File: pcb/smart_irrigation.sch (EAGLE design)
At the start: 33 parts, among them IC1 TMP36, IC2 7805DT, IC3 7833DT, IC4 DS1307, Q1 IRF730, Q2 32.768, T1 2N3904, U1 BL600

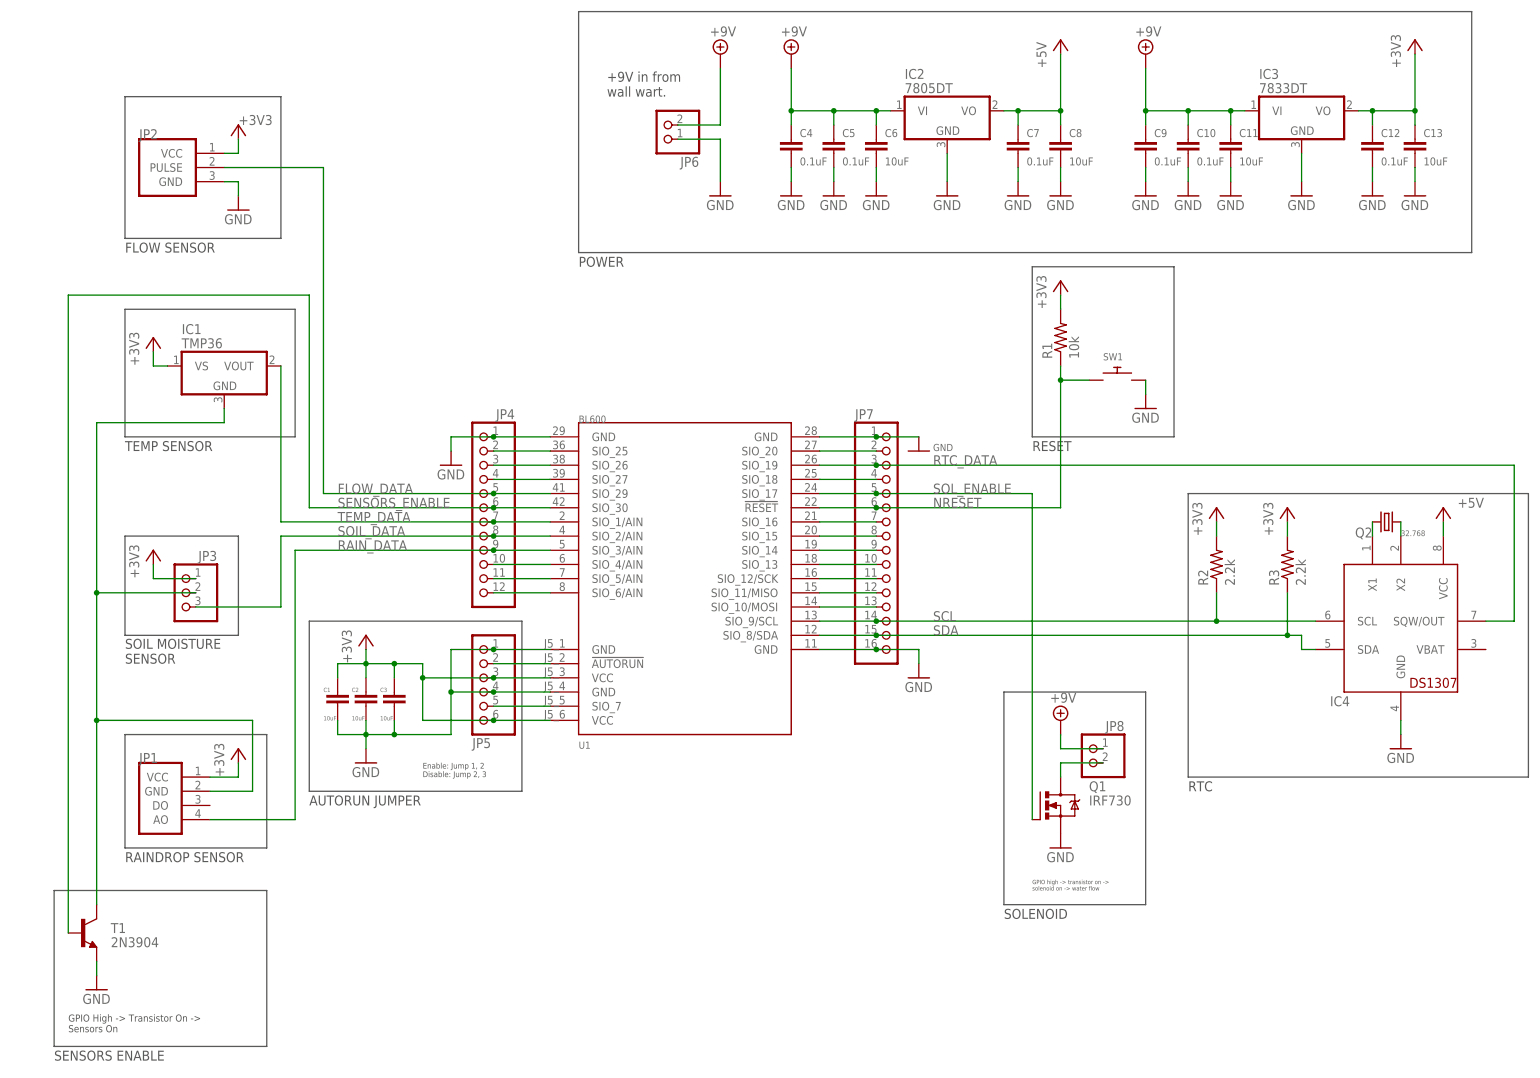
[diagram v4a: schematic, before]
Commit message: PCB: Change sensor pin assignments
All digital sensor outputs are now in one cluster and all analog sensor
outputs are in another cluster.
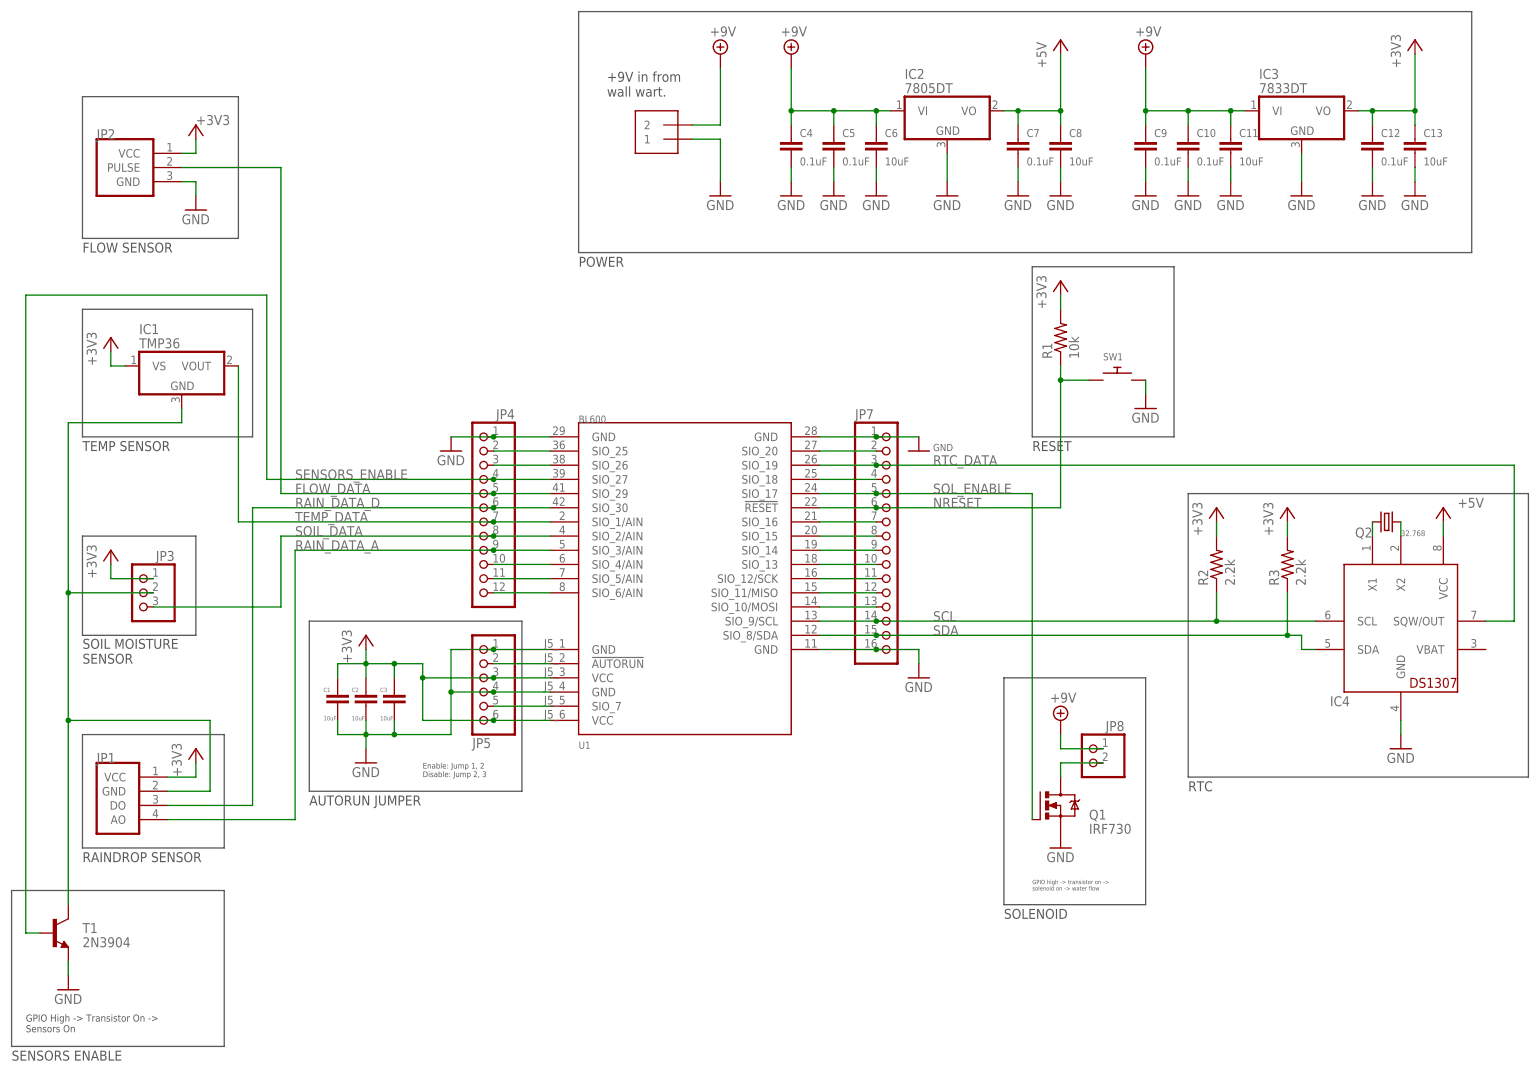
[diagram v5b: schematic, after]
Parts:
- JP6: value (none) -> 1X2-3.5MM; device pinhead:PINHD-1X2 -> adafruit:1X2-3.5MM
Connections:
- net RAIN_DATA renamed RAIN_DATA_A
- removed net SIO_27: JP4.4, U1.SIO_27
- new net RAIN_DATA_D: JP1.DO, JP4.6, U1.SIO_30
- net SENSORS_ENABLE: now also JP4.4, U1.SIO_27; no longer JP4.6, U1.SIO_30
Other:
- moved on the sheet: IC1, JP1, JP2, JP3, T1

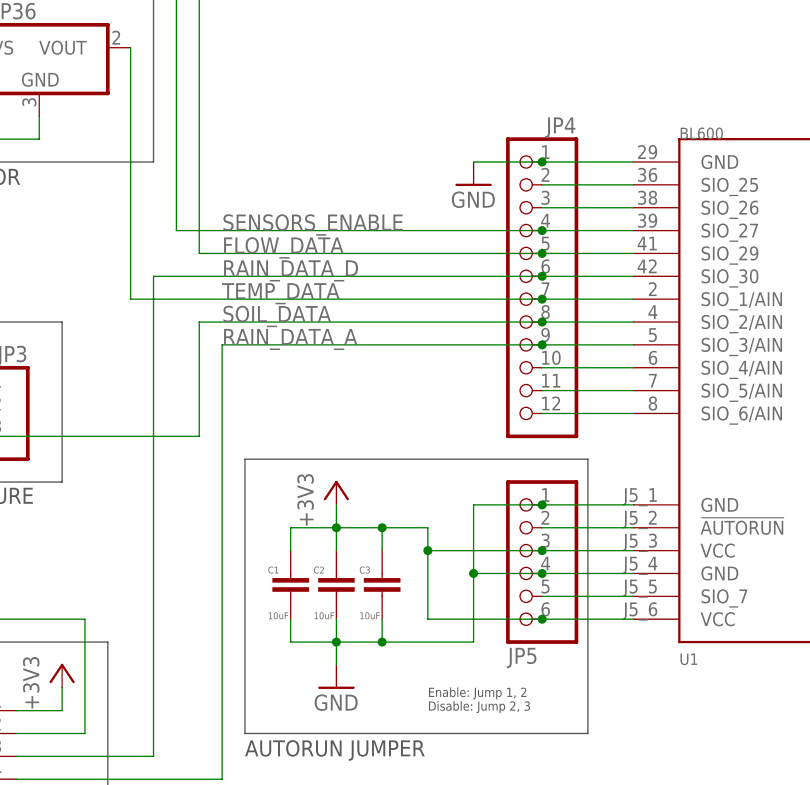
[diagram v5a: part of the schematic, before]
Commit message: PCB: Change SENSORS_ENABLE signal pin
The BL600 breakout board includes SIO_26 and SIO_27, but they're
reserved and unusable for some reason. SENSORS_ENABLE was thus changed
from SIO_27 to SIO_25.
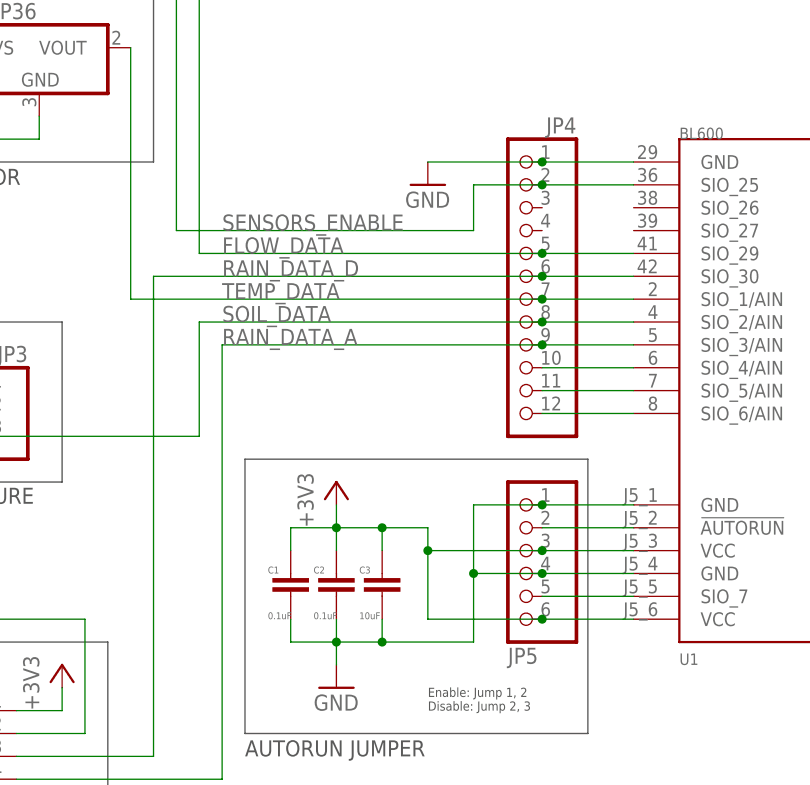
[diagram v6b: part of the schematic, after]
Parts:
- C1, C2: value 10uF -> 0.1uF
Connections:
- removed net SIO_25: JP4.2, U1.SIO_25
- removed net SIO_26: JP4.3, U1.SIO_26
- net SENSORS_ENABLE: now also JP4.2, U1.SIO_25; no longer JP4.4, U1.SIO_27
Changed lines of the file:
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@@
 <?xml version="1.0" encoding="utf-8"?>
 <!DOCTYPE eagle SYSTEM "eagle.dtd">
-<eagle version="7.3.0">
+<eagle version="7.5.0">
 <drawing>
 <settings>
@@
 <part name="GND4" library="supply1" deviceset="GND" device=""/>
 <part name="GND9" library="supply1" deviceset="GND" device=""/>
-<part name="C1" library="rcl" deviceset="C-EU" device="C0805" value="10uF"/>
-<part name="C2" library="rcl" deviceset="C-EU" device="C0805" value="10uF"/>
+<part name="C1" library="rcl" deviceset="C-EU" device="C0805" value="0.1uF"/>
+<part name="C2" library="rcl" deviceset="C-EU" device="C0805" value="0.1uF"/>
 <part name="C3" library="rcl" deviceset="C-EU" device="C0805" value="10uF"/>
 <part name="JP2" library="smart_irrigation" deviceset="FLOW" device=""/>
@@
 <instance part="JP1" gate="A" x="20.32" y="66.04"/>
 <instance part="+3V34" gate="G$1" x="35.56" y="76.2"/>
-<instance part="GND4" gate="1" x="81.28" y="129.54"/>
+<instance part="GND4" gate="1" x="76.2" y="129.54"/>
 <instance part="GND9" gate="1" x="165.1" y="129.54" smashed="yes">
 <attribute name="VALUE" x="167.64" y="129.54" size="1.27" layer="96"/>
@@
 <wire x1="99.06" y1="132.08" x2="88.9" y2="132.08" width="0.1524" layer="91"/>
 <junction x="88.9" y="132.08"/>
-<wire x1="81.28" y1="132.08" x2="88.9" y2="132.08" width="0.1524" layer="91"/>
+<wire x1="76.2" y1="132.08" x2="88.9" y2="132.08" width="0.1524" layer="91"/>
 <pinref part="GND4" gate="1" pin="GND"/>
 </segment>
@@
 </segment>
 </net>
-<net name="SIO_25" class="0">
-<segment>
-<pinref part="JP4" gate="G$1" pin="2"/>
-<pinref part="U1" gate="G$1" pin="SIO_25"/>
-<wire x1="88.9" y1="129.54" x2="99.06" y2="129.54" width="0.1524" layer="91"/>
-</segment>
-</net>
-<net name="SIO_26" class="0">
-<segment>
-<pinref part="U1" gate="G$1" pin="SIO_26"/>
-<pinref part="JP4" gate="G$1" pin="3"/>
-<wire x1="99.06" y1="127" x2="88.9" y2="127" width="0.1524" layer="91"/>
-</segment>
-</net>
 <net name="FLOW_DATA" class="0">
 <segment>
@@
 <segment>
 <wire x1="48.26" y1="157.48" x2="5.08" y2="157.48" width="0.1524" layer="91"/>
-<wire x1="48.26" y1="157.48" x2="48.26" y2="124.46" width="0.1524" layer="91"/>
-<wire x1="48.26" y1="124.46" x2="88.9" y2="124.46" width="0.1524" layer="91"/>
-<pinref part="JP4" gate="G$1" pin="4"/>
-<pinref part="U1" gate="G$1" pin="SIO_27"/>
-<wire x1="88.9" y1="124.46" x2="99.06" y2="124.46" width="0.1524" layer="91"/>
-<junction x="88.9" y="124.46"/>
-<label x="53.34" y="124.46" size="1.778" layer="95"/>
 <wire x1="5.08" y1="157.48" x2="5.08" y2="43.18" width="0.1524" layer="91"/>
 <pinref part="T1" gate="G1" pin="B"/>
 <wire x1="5.08" y1="43.18" x2="7.62" y2="43.18" width="0.1524" layer="91"/>
+<wire x1="48.26" y1="157.48" x2="48.26" y2="124.46" width="0.1524" layer="91"/>
+<wire x1="48.26" y1="124.46" x2="81.28" y2="124.46" width="0.1524" layer="91"/>
+<wire x1="81.28" y1="124.46" x2="81.28" y2="129.54" width="0.1524" layer="91"/>
+<pinref part="U1" gate="G$1" pin="SIO_25"/>
+<pinref part="JP4" gate="G$1" pin="2"/>
+<wire x1="88.9" y1="129.54" x2="99.06" y2="129.54" width="0.1524" layer="91"/>
+<wire x1="81.28" y1="129.54" x2="88.9" y2="129.54" width="0.1524" layer="91"/>
+<junction x="88.9" y="129.54"/>
+<label x="53.34" y="124.46" size="1.778" layer="95"/>
 </segment>
 </net>

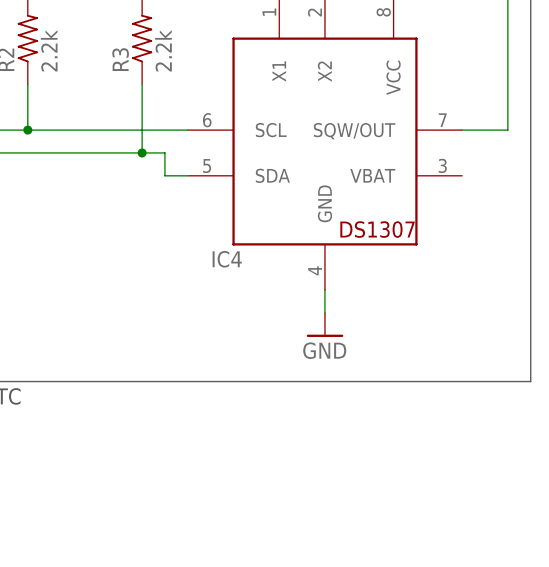
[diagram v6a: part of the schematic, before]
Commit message: PCB: Ground VBAT pin of RTC
Per datasheet, if VBAT is unused, it must be grounded.
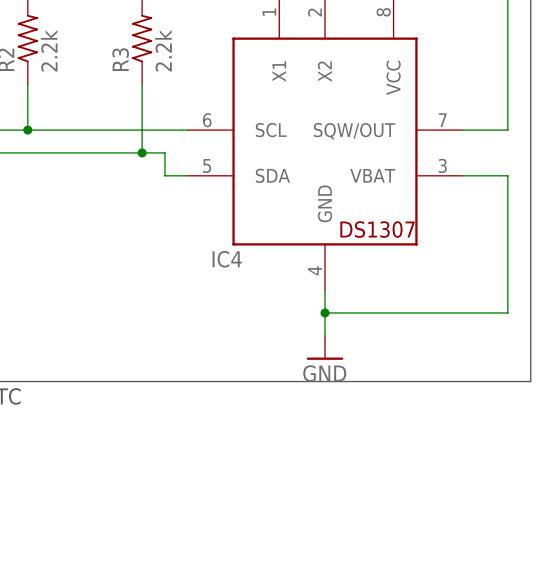
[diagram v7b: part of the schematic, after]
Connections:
- net GND: now also IC4.VBAT
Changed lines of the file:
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@@
 <attribute name="VALUE" x="261.62" y="119.38" size="1.778" layer="96"/>
 </instance>
-<instance part="GND21" gate="1" x="251.46" y="76.2"/>
+<instance part="GND21" gate="1" x="251.46" y="73.66"/>
 <instance part="Q2" gate="G$1" x="248.92" y="116.84" smashed="yes" rot="R180">
 <attribute name="NAME" x="246.38" y="115.824" size="1.778" layer="95" rot="R180"/>
@@
 <pinref part="GND21" gate="1" pin="GND"/>
 <pinref part="IC4" gate="G$1" pin="GND"/>
+<wire x1="251.46" y1="76.2" x2="251.46" y2="78.74" width="0.1524" layer="91"/>
+<pinref part="IC4" gate="G$1" pin="VBAT"/>
 <wire x1="251.46" y1="78.74" x2="251.46" y2="81.28" width="0.1524" layer="91"/>
+<wire x1="266.7" y1="93.98" x2="271.78" y2="93.98" width="0.1524" layer="91"/>
+<wire x1="271.78" y1="93.98" x2="271.78" y2="78.74" width="0.1524" layer="91"/>
+<wire x1="251.46" y1="78.74" x2="271.78" y2="78.74" width="0.1524" layer="91"/>
+<junction x="251.46" y="78.74"/>
 </segment>
 <segment>

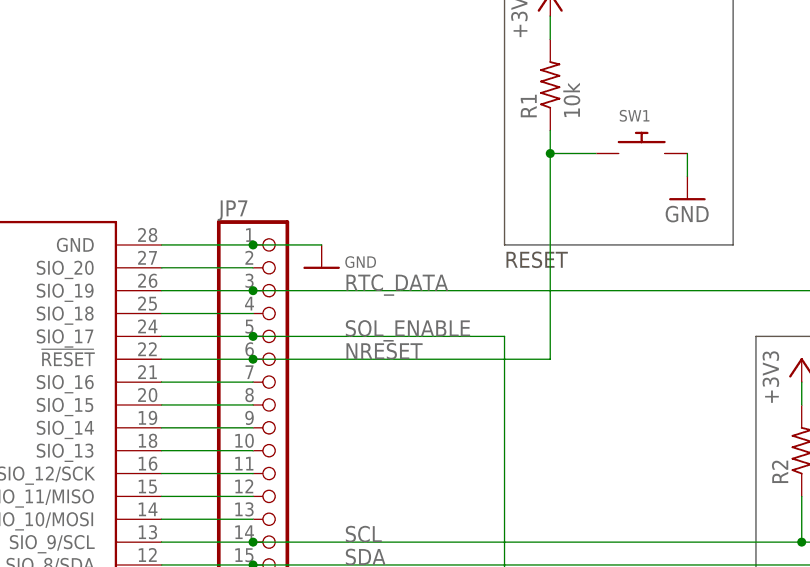
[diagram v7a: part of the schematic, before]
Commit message: PCB: Rename RTC_DATA to RTC_SQW
The signal is actually a square wave, not any sort of data.
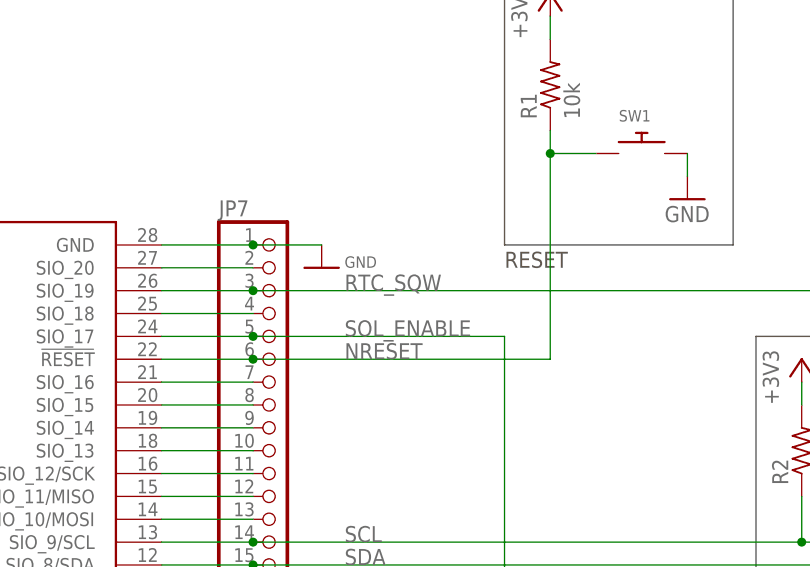
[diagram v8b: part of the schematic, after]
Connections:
- net RTC_DATA renamed RTC_SQW
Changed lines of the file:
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@@
 <setting verticaltext="up"/>
 </settings>
-<grid distance="0.1" unitdist="inch" unit="inch" style="lines" multiple="1" display="yes" altdistance="0.01" altunitdist="inch" altunit="inch"/>
+<grid distance="0.1" unitdist="inch" unit="inch" style="lines" multiple="1" display="no" altdistance="0.01" altunitdist="inch" altunit="inch"/>
 <layers>
 <layer number="1" name="Top" color="4" fill="1" visible="no" active="no"/>
@@
 </segment>
 </net>
-<net name="RTC_DATA" class="0">
+<net name="RTC_SQW" class="0">
 <segment>
 <pinref part="U1" gate="G$1" pin="SIO_19"/>
